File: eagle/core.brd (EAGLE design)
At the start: 36.8 x 19.1 mm, 19 parts, among them K1 AQH2223A, SW0 TPTP10R, SW1 TPTP10R

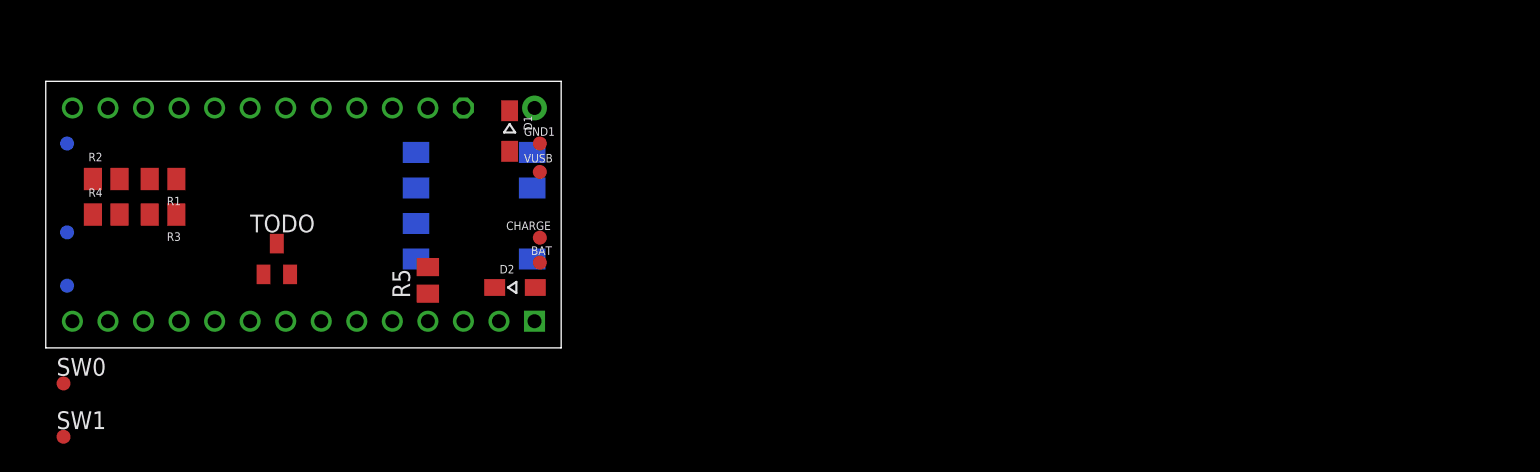
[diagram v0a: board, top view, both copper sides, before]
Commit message: add torch and uv schematic
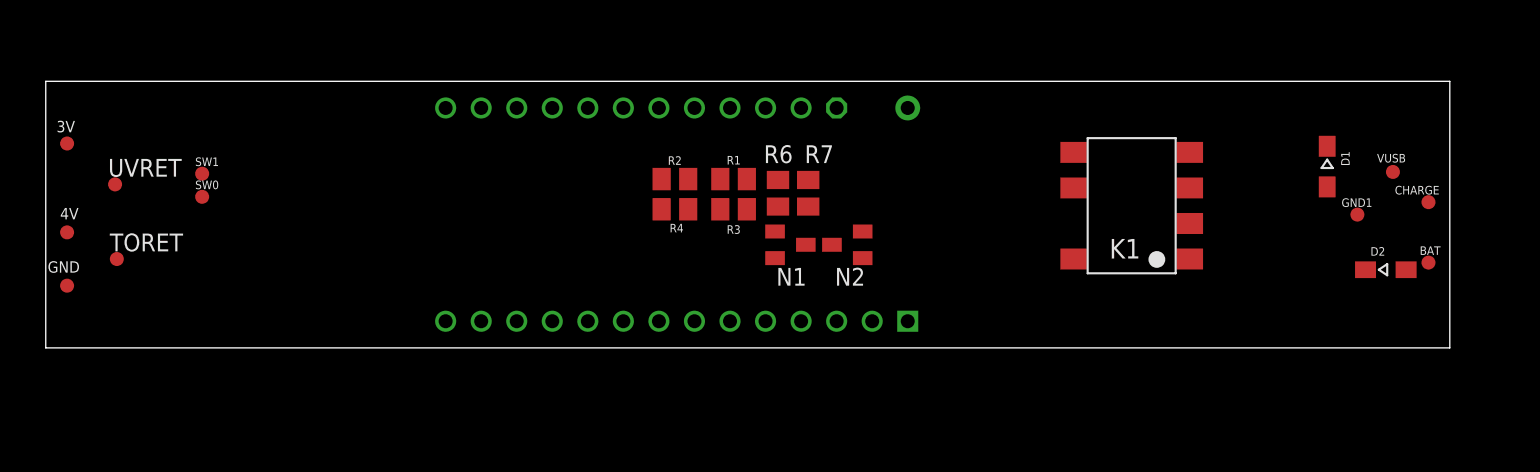
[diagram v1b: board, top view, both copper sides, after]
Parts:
- removed R5: 10k, resistor:M0805
- removed TODO: BC846, transistor:SOT23
- added N1, N2: BC846, transistor:SOT23
- added R6, R7: 1k, resistor:M0805
- added TORET, UVRET: TPTP10R, testpad:TP10R
- moved CHARGE 63.6 mm to (98.8, 10.4)
- moved BAT 63.5 mm to (98.8, 6.10)
- moved D2 62.2 mm to (95.8, 5.59)
- moved VUSB 61.0 mm to (96.3, 12.6)
- moved GND1 58.6 mm to (93.7, 9.53)
- moved D1 58.5 mm to (91.6, 13.0)
- moved K1 47.0 mm to (77.6, 10.2), flipped to the top
- moved R3 40.8 mm to (49.1, 9.91)
- moved R1 40.8 mm to (49.1, 12.1)
- moved R4 40.6 mm to (45.0, 9.91)
- moved R2 40.6 mm to (45.0, 12.1)
- moved U$1 26.7 mm to (45.1, 9.53)
- moved SW1 21.2 mm to (11.2, 12.4)
- moved SW0 16.6 mm to (11.2, 10.8)
- flipped 3V to the top
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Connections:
- removed net BATSIG: R5.2
- removed net N$3: R5.1, U$1.2-OUT2
- new net N$10: N1.1, R6.1
- new net N$11: N2.1, R7.1
- new net N$12: N1.2, UVRET.TP
- new net N$13: N2.2, TORET.TP
- new net N$8: R7.2, U$1.23-A9/CRX1/CCLK1
- new net N$9: R6.2, U$1.22-A8/CTX1
- net 3V: now also N1.3, N2.3
- net 4V: no longer SW1.TP
- net N$2: now also U$1.21-A7/RX5/BCLK1; no longer U$1.15-A1/RX3/S-PDIF_IN
- net N$5: no longer SW0.TP
- net N$6: now also U$1.20-A6/TX5/LRCLK1; no longer U$1.14-A0/TX3/S-PFI_OUT
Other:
- board size 36.8 x 19.1 mm -> 100.3 x 19.1 mm

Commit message: Display board redesigned with FFC connector
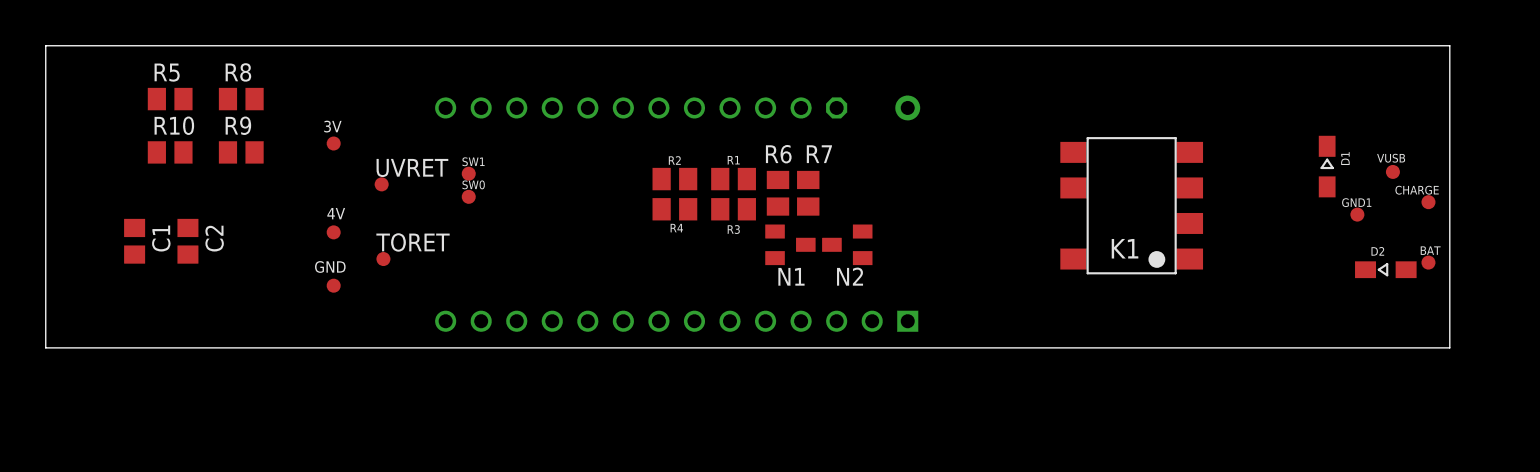
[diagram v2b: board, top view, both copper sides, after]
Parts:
- added C1, C2: 0.1u, resistor:C0805
- added R10, R5: 10k, resistor:M0805
- added R8, R9: 100k, resistor:M0805
- moved 3V 19.1 mm to (20.6, 14.6)
- moved 4V 19.1 mm to (20.6, 8.26)
- moved GND 19.1 mm to (20.6, 4.45)
- moved UVRET 19.1 mm to (24.0, 11.7)
- moved SW0 19.0 mm to (30.2, 10.8)
- moved SW1 19.0 mm to (30.2, 12.4)
- moved TORET 19.0 mm to (24.1, 6.35)
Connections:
- new net ENCL: R5.2, R8.1
- new net ENCPINL: C1.1, R5.1
- new net ENCPINR: C2.1, R10.1
- new net ENCR: R10.2, R9.1
- net 3V: now also R8.2, R9.2
- net GND: now also C1.2, C2.2
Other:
- board size 100.3 x 19.1 mm -> 100.3 x 21.6 mm

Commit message: ffc breakout and core changes
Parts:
- removed 3V, 4V, BAT, CHARGE, GND, GND1, SW0, SW1, TORET, UVRET, VUSB: TPTP10R, testpad:TP10R
- removed D1, D2: 1N5817WS, general:SOD323-W
- removed K1: AQH2223A, relay:DIL07SMD
- removed N1, N2: BC846, transistor:SOT23
- added C3, C4: 10u, resistor:C0805
- added ENCL, ENCR, MBTN, SBTN, TODO, TODO1: TPTP10R, testpad:TP10R
- added R11, R12: 10k, resistor:M0805
- added U$2: TEENSYSMALL, general:TEENSYSMALL
- added U$3: 16PINFFC, general:16PINFFC
- R1, R2, R3, R4: value 100k -> 20M
- R6, R7: value 1k -> 10k
- R8, R9: value 100k -> 10k
- U$1: value TEENSY40EDGES -> TEENSY4; device general:TEENSY40 -> general:TEENSYSMALL
- moved C1 80.9 mm to (87.0, 1.27), flipped to the bottom, turned to 0 degrees
- moved R5 79.1 mm to (87.0, 5.08), flipped to the bottom, turned to 180 degrees
- moved R10 74.8 mm to (83.2, 5.08), flipped to the bottom
- moved R8 73.7 mm to (87.0, 7.62), flipped to the bottom
- moved C2 73.3 mm to (83.2, 1.27), flipped to the bottom, turned to 180 degrees
- moved R9 69.5 mm to (83.2, 7.62), flipped to the bottom, turned to 180 degrees
- moved U$1 36.2 mm to (81.3, 10.8), flipped to the top, turned to 180 degrees
- moved R4 25.7 mm to (69.2, 1.27), turned to 180 degrees
- moved R2 23.1 mm to (65.4, 1.27)
- moved R6 20.7 mm to (73.0, 11.4), flipped to the bottom
- moved R3 20.6 mm to (69.2, 5.08), turned to 0 degrees
- moved R1 17.7 mm to (65.4, 5.08)
- moved R7 16.0 mm to (70.5, 11.4), flipped to the bottom, turned to 270 degrees
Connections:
- removed net N$1: K1.2
- removed net N$10: N1.1, R6.1
- removed net N$11: N2.1, R7.1
- removed net N$12: N1.2, UVRET.TP
- removed net N$13: N2.2, TORET.TP
- removed net N$2: R3.2, R4.2, U$1.21-A7/RX5/BCLK1
- removed net N$4: BAT.TP, D2.A
- removed net N$5: D2.C, K1.8
- removed net N$6: R1.2, R2.2, U$1.20-A6/TX5/LRCLK1
- removed net N$7: K1.3
- removed net N$8: R7.2, U$1.23-A9/CRX1/CCLK1
- removed net N$9: R6.2, U$1.22-A8/CTX1
- removed net VUSB: CHARGE.TP, D1.A, R1.1, VUSB.TP
- new net ANTT1: R1.1, R2.2, U$1.14
- new net ANTT2: R3.1, R4.2, U$1.15
- new net BCLK: U$3.12
- new net DC: U$3.5
- new net DOUT: U$3.11
- new net LRCL: U$3.10
- new net MBTN: MBTN.TP, R11.1, R12.2
- new net MBTNPIN: C4.1, R12.1, TODO.TP
- new net MOSI: U$3.3
- new net PWM1: U$1.5, U$3.16
- new net PWM2: U$1.4, U$3.15
- new net PWM3: U$1.3, U$3.14
- new net PWM4: U$1.2, U$3.13
- new net SBTN: R6.1, R7.2, SBTN.TP
- new net SBTNPIN: C3.1, R7.1, TODO1.TP
- new net SCK: U$3.4
- new net SSCL: U$3.2
- new net SSDA: U$3.1
- new net T4RX: U$1.0, U$2.1
- new net T4TX: U$1.1, U$2.0
- new net TFTCS: U$3.7
- new net TFTRST: U$3.6
- net 3V: now also R1.2, R11.2, R3.2, R6.2, U$1.3V, U$2.3V; no longer 3V.TP, N1.3, N2.3, U$1.3V3-1
- net 4V: no longer 4V.TP, D1.C, K1.6, R3.1
- net ENCL: now also ENCL.TP
- net ENCPINL: now also U$2.3
- net ENCPINR: now also U$2.4
- net ENCR: now also ENCR.TP
- net GND: now also C3.2, C4.2, U$1.GND, U$2.GND, U$3.BASE1, U$3.BASE2; no longer GND.TP, GND1.TP, U$1.GND1
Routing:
- net 3V: track 0.00 -> 35.7 mm, vias 0 -> 1
- net ENCR: track 0.00 -> 30.8 mm
- net PWM1: track 0.00 -> 25.0 mm, vias 0 -> 2
- net PWM2: track 0.00 -> 22.2 mm, vias 0 -> 2
- net T4TX: track 0.00 -> 19.9 mm, vias 0 -> 1
- net PWM3: track 0.00 -> 19.5 mm, vias 0 -> 2
- net ENCL: track 0.00 -> 17.6 mm
- net T4RX: track 0.00 -> 17.0 mm, vias 0 -> 1
- net PWM4: track 0.00 -> 16.7 mm, vias 0 -> 2
- net ENCPINR: track 0.00 -> 4.60 mm
- net ENCPINL: track 0.00 -> 4.60 mm
- net ANTT2: track 0.00 -> 4.07 mm
- net ANTT1: track 0.00 -> 4.07 mm
- net GND: track 0.00 -> 3.81 mm, vias 0 -> 2
- added copper zone on layer 1, net GND
- added copper zone on layer 16, net GND
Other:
- board size 100.3 x 21.6 mm -> 38.7 x 21.6 mm

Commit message: mini probe
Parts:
- removed U$3: 16PINFFC, general:16PINFFC
- added 3V, BCLK, DOUT, GND, L1-, L2-, L3-, L4-, LRCL, SSCL, SSDA: TPTP16R, testpad:TP16R
- added IC5: APX803, adafruit:SOT23
- added LED1: (no value), led:LED3MM
- added R13: 10K, microbuilder:0603-NO
- added R14: 22, microbuilder:0603-NO
- added R15, R16, R17, R18: (no value), resistor:R0805
- added T1, T2, T3, T4: BC846, transistor:SOT23
- added U$4: TFT, general:MICROBUILDER_TFT_1.14IN_240X135_WRAPUNDER
- moved U$1 48.3 mm to (33.0, 9.84), flipped to the bottom, turned to 0 degrees
- moved C2 40.7 mm to (43.2, 8.89), turned to 0 degrees
- moved R10 40.5 mm to (43.2, 11.4)
- moved R9 40.5 mm to (43.2, 14.0)
- moved C1 40.1 mm to (47.6, 8.89), turned to 180 degrees
- moved ENCL 40.0 mm to (59.1, 1.27)
- moved ENCR 40.0 mm to (59.1, 3.17)
- moved MBTN 40.0 mm to (59.1, 5.08)
- moved SBTN 40.0 mm to (59.1, 6.99)
- moved R5 39.9 mm to (47.6, 11.4)
- moved R8 39.9 mm to (47.6, 14.0)
- moved R2 31.3 mm to (94.0, 14.0)
- moved TODO1 29.3 mm to (33.7, 10.8)
- moved R4 29.1 mm to (96.5, 11.4)
- moved TODO 26.7 mm to (36.2, 11.4)
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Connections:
- new net !TFTRST: IC5.2, R13.1
- new net L1-: L1-.TP, T1.3
- new net L2-: L2-.TP, T2.3
- new net L3-: L3-.TP, T3.3
- new net L4-: L4-.TP, LED1.K, T4.3
- new net N$1: R14.2, U$4.11
- new net N$2: R15.2, T1.1
- new net N$3: R16.2, T2.1
- new net N$4: R17.2, T3.1
- new net N$5: R18.2, T4.1
- net 3V: now also 3V.TP, IC5.3, LED1.A, R13.2, U$4.10, U$4.12
- net BCLK: now also BCLK.TP; no longer U$3.12
- net DC: now also U$1.9, U$4.5; no longer U$3.5
- net DOUT: now also DOUT.TP; no longer U$3.11
- net GND: now also GND.TP, IC5.1, R14.1, T1.2, T2.2, T3.2, T4.2, U$4.13, U$4.8; no longer U$3.BASE1, U$3.BASE2
- net LRCL: now also LRCL.TP; no longer U$3.10
- net MOSI: now also U$1.11, U$4.3; no longer U$3.3
- net PWM1: now also R15.1; no longer U$3.16
- net PWM2: now also R16.1; no longer U$3.15
- net PWM3: now also R17.1; no longer U$3.14
- net PWM4: now also R18.1; no longer U$3.13
- net SCK: now also U$1.13, U$4.4; no longer U$3.4
- net SSCL: now also SSCL.TP; no longer U$3.2
- net SSDA: now also SSDA.TP; no longer U$3.1
- net TFTCS: now also U$1.10, U$4.7; no longer U$3.7
- net TFTRST: now also U$1.7, U$4.6; no longer U$3.6
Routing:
- net 3V: track 35.7 -> 0.00 mm, vias 1 -> 0
- net ENCR: track 30.8 -> 0.00 mm
- net PWM1: track 25.0 -> 0.00 mm, vias 2 -> 0
- net PWM2: track 22.2 -> 0.00 mm, vias 2 -> 0
- net T4TX: track 19.9 -> 0.00 mm, vias 1 -> 0
- net PWM3: track 19.5 -> 0.00 mm, vias 2 -> 0
- net ENCL: track 17.6 -> 0.00 mm
- net T4RX: track 17.0 -> 0.00 mm, vias 1 -> 0
- net PWM4: track 16.7 -> 0.00 mm, vias 2 -> 0
- net ENCPINR: track 4.60 -> 0.00 mm
- net ENCPINL: track 4.60 -> 0.00 mm
- net ANTT2: track 4.07 -> 0.00 mm
- net ANTT1: track 4.07 -> 0.00 mm
- net GND: track 3.81 -> 0.00 mm, vias 2 -> 0
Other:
- board size 38.7 x 21.6 mm -> 103.5 x 19.7 mm

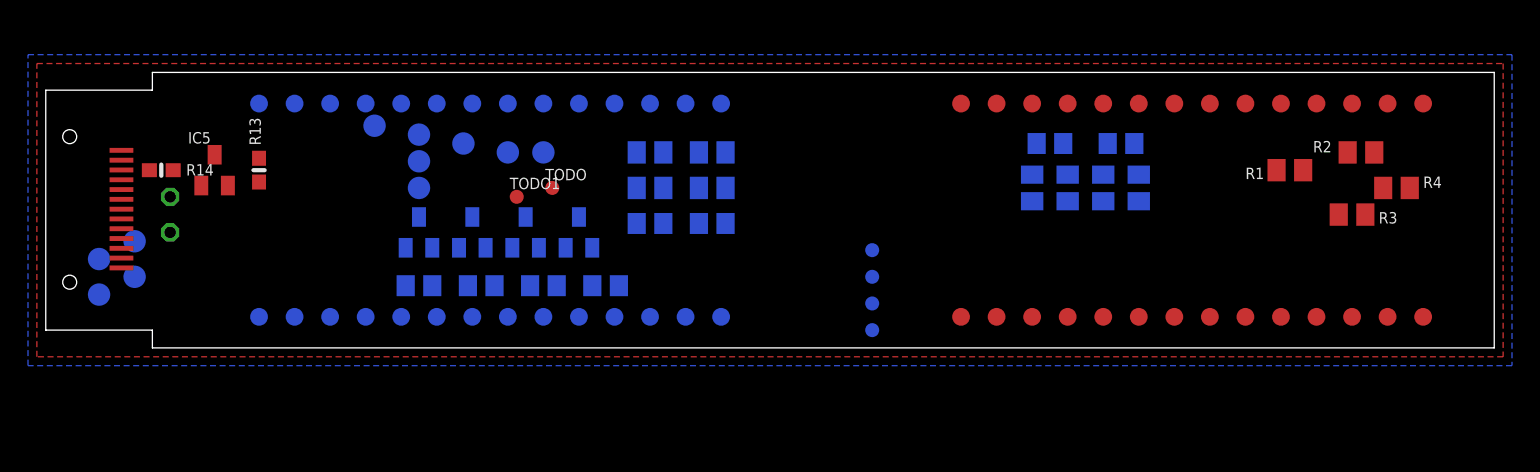
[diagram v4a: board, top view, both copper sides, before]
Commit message: decided on ffc wire layout.
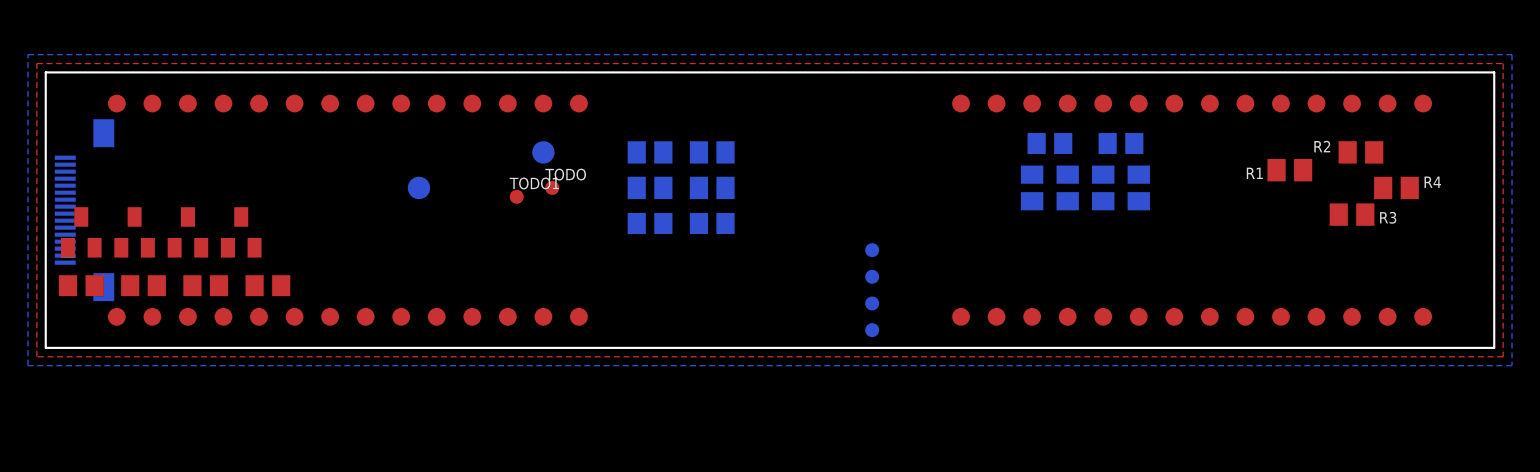
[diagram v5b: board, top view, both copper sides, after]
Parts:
- removed BCLK, DOUT, L1-, L2-, L3-, L4-, LRCL, SSCL, SSDA: TPTP16R, testpad:TP16R
- removed IC5: APX803, adafruit:SOT23
- removed LED1: (no value), led:LED3MM
- removed R13: 10K, microbuilder:0603-NO
- removed R14: 22, microbuilder:0603-NO
- removed U$4: TFT, general:MICROBUILDER_TFT_1.14IN_240X135_WRAPUNDER
- added U$3: 16PINFFC, general:16PINFFC
- moved R15 24.1 mm to (2.54, 4.45), flipped to the top, turned to 180 degrees
- moved R17 24.1 mm to (11.4, 4.45), flipped to the top, turned to 180 degrees
- moved R18 24.1 mm to (15.9, 4.45), flipped to the top, turned to 180 degrees
- moved T1 24.1 mm to (2.54, 8.26), flipped to the top
- moved T2 24.1 mm to (6.35, 8.26), flipped to the top
- moved T4 24.1 mm to (14.0, 8.26), flipped to the top
- moved R16 24.1 mm to (6.99, 4.45), flipped to the top, turned to 180 degrees
- moved T3 24.1 mm to (10.2, 8.26), flipped to the top
- moved U$1 12.7 mm to (20.3, 9.84), flipped to the top
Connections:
- removed net !TFTRST: IC5.2, R13.1
- removed net N$1: R14.2, U$4.11
- removed net SSCL: SSCL.TP
- removed net SSDA: SSDA.TP
- new net SCL: U$1.19, U$3.12
- new net SDA: U$1.18, U$3.11
- net 3V: now also U$3.13; no longer IC5.3, LED1.A, R13.2, U$4.10, U$4.12
- net BCLK: now also U$1.21; no longer BCLK.TP
- net DC: now also U$3.7; no longer U$4.5
- net DOUT: now also U$1.8, U$3.6; no longer DOUT.TP
- net ENCPINL: no longer U$2.3
- net ENCPINR: no longer U$2.4
- net GND: now also U$3.14, U$3.BASE1, U$3.BASE2; no longer IC5.1, R14.1, U$4.13, U$4.8
- net L1-: now also U$3.1; no longer L1-.TP
- net L2-: now also U$3.2; no longer L2-.TP
- net L3-: now also U$3.3; no longer L3-.TP
- net L4-: now also U$3.4; no longer L4-.TP, LED1.K
- net LRCL: now also U$1.20; no longer LRCL.TP
- net MOSI: now also U$3.9; no longer U$4.3
- net PWM1: now also U$1.2; no longer U$1.5
- net PWM2: now also U$1.3; no longer U$1.4
- net PWM3: now also U$1.4; no longer U$1.3
- net PWM4: now also U$1.5; no longer U$1.2
- net SCK: now also U$3.10; no longer U$4.4
- net TFTCS: now also U$3.8; no longer U$4.7
- net TFTRST: now also U$3.5; no longer U$4.6
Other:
- outline, holes or cut-outs redrawn

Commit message: First order of probe, probebase and FFC breakout PCBs for 22mm enclosure
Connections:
- net 3V: now also U$3.15; no longer U$3.13
- net BCLK: now also U$3.14
- net GND: now also U$3.16; no longer U$3.14
- net LRCL: now also U$3.13
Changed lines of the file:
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@@
 <contactref element="T4" pad="2"/>
 <contactref element="GND" pad="TP"/>
-<contactref element="U$3" pad="14"/>
 <contactref element="U$3" pad="BASE2"/>
 <contactref element="U$3" pad="BASE1"/>
+<contactref element="U$3" pad="16"/>
+<wire x1="93.03" y1="13.97" x2="97.47" y2="11.43" width="0" layer="19" extent="1-1"/>
+<wire x1="77.785" y1="14.605" x2="93.03" y2="13.97" width="0" layer="19" extent="1-16"/>
+<wire x1="70.805" y1="14.605" x2="77.785" y2="14.605" width="0" layer="19" extent="16-16"/>
+<wire x1="65.405" y1="2.22" x2="70.805" y2="14.605" width="0" layer="19" extent="1-16"/>
+<wire x1="48.575" y1="8.89" x2="65.405" y2="2.22" width="0" layer="19" extent="1-16"/>
+<wire x1="42.23" y1="8.89" x2="48.575" y2="8.89" width="0" layer="19" extent="16-16"/>
+<wire x1="35.56" y1="13.97" x2="42.23" y2="8.89" width="0" layer="19" extent="16-16"/>
+<wire x1="14.92" y1="7.155" x2="35.56" y2="13.97" width="0" layer="19" extent="1-16"/>
+<wire x1="11.11" y1="7.155" x2="14.92" y2="7.155" width="0" layer="19" extent="1-1"/>
+<wire x1="7.3" y1="7.155" x2="11.11" y2="7.155" width="0" layer="19" extent="1-1"/>
+<wire x1="3.49" y1="7.155" x2="7.3" y2="7.155" width="0" layer="19" extent="1-1"/>
+<wire x1="4.147" y1="4.34" x2="3.49" y2="7.155" width="0" layer="19" extent="1-16"/>
 <wire x1="5.08" y1="2.22" x2="4.147" y2="4.34" width="0" layer="19" extent="1-16"/>
+<wire x1="1.397" y1="13.59" x2="3.49" y2="7.155" width="0" layer="19" extent="1-16"/>
+<wire x1="4.147" y1="15.34" x2="1.397" y2="13.59" width="0" layer="19" extent="16-16"/>
 </signal>
 <signal name="3V">
@@
 <contactref element="R11" pad="2"/>
 <contactref element="3V" pad="TP"/>
-<contactref element="U$3" pad="13"/>
+<contactref element="U$3" pad="15"/>
 <wire x1="87.95" y1="12.7" x2="94.295" y2="9.525" width="0" layer="19" extent="1-1"/>
 <wire x1="75.565" y1="12.38" x2="87.95" y2="12.7" width="0" layer="19" extent="1-16"/>
@@
 <wire x1="26.67" y1="11.43" x2="44.13" y2="13.97" width="0" layer="19" extent="16-16"/>
 <wire x1="10.16" y1="17.46" x2="26.67" y2="11.43" width="0" layer="19" extent="1-16"/>
-<wire x1="1.397" y1="12.09" x2="10.16" y2="17.46" width="0" layer="19" extent="1-16"/>
+<wire x1="1.397" y1="13.09" x2="10.16" y2="17.46" width="0" layer="19" extent="1-16"/>
 </signal>
 <signal name="ENCL">
@@
 <signal name="BCLK">
 <contactref element="U$1" pad="21"/>
+<contactref element="U$3" pad="14"/>
+<wire x1="1.397" y1="12.59" x2="17.78" y2="17.46" width="0" layer="19" extent="1-16"/>
 </signal>
 <signal name="DOUT">
@@
 <signal name="LRCL">
 <contactref element="U$1" pad="20"/>
+<contactref element="U$3" pad="13"/>
+<wire x1="1.397" y1="12.09" x2="20.32" y2="17.46" width="0" layer="19" extent="1-16"/>
 </signal>
 <signal name="SDA">
